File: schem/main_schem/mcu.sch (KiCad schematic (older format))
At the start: 40 parts, among them P2 CONN_PORTD, P3 CONN_ICD, P4 CONN_NFC, P5 CONN_2, Q2 NPN, SW1 SW_RESET, U4 25LC256, U5 PIC18F97J60, X1 25MHz

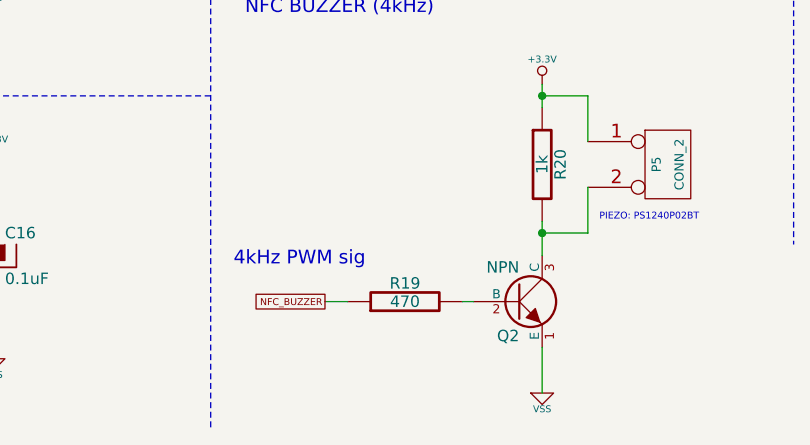
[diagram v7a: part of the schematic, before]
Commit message: Update parts list, update netlist, start associating footprints
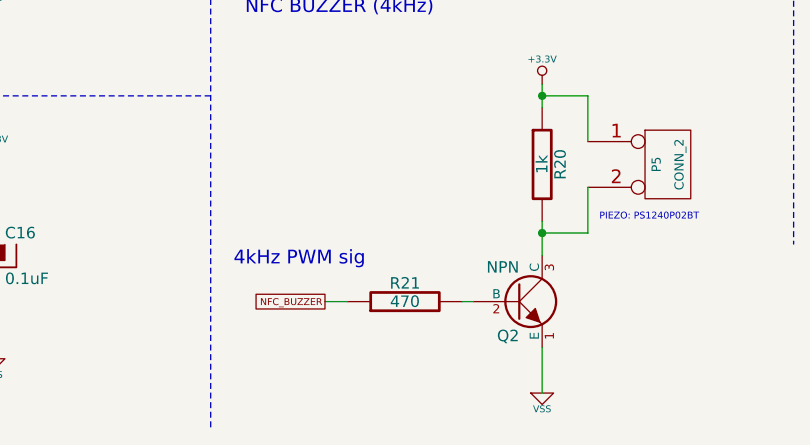
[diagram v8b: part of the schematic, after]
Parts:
- renumbered R19 to R21
